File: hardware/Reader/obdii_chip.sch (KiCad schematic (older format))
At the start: 29 parts

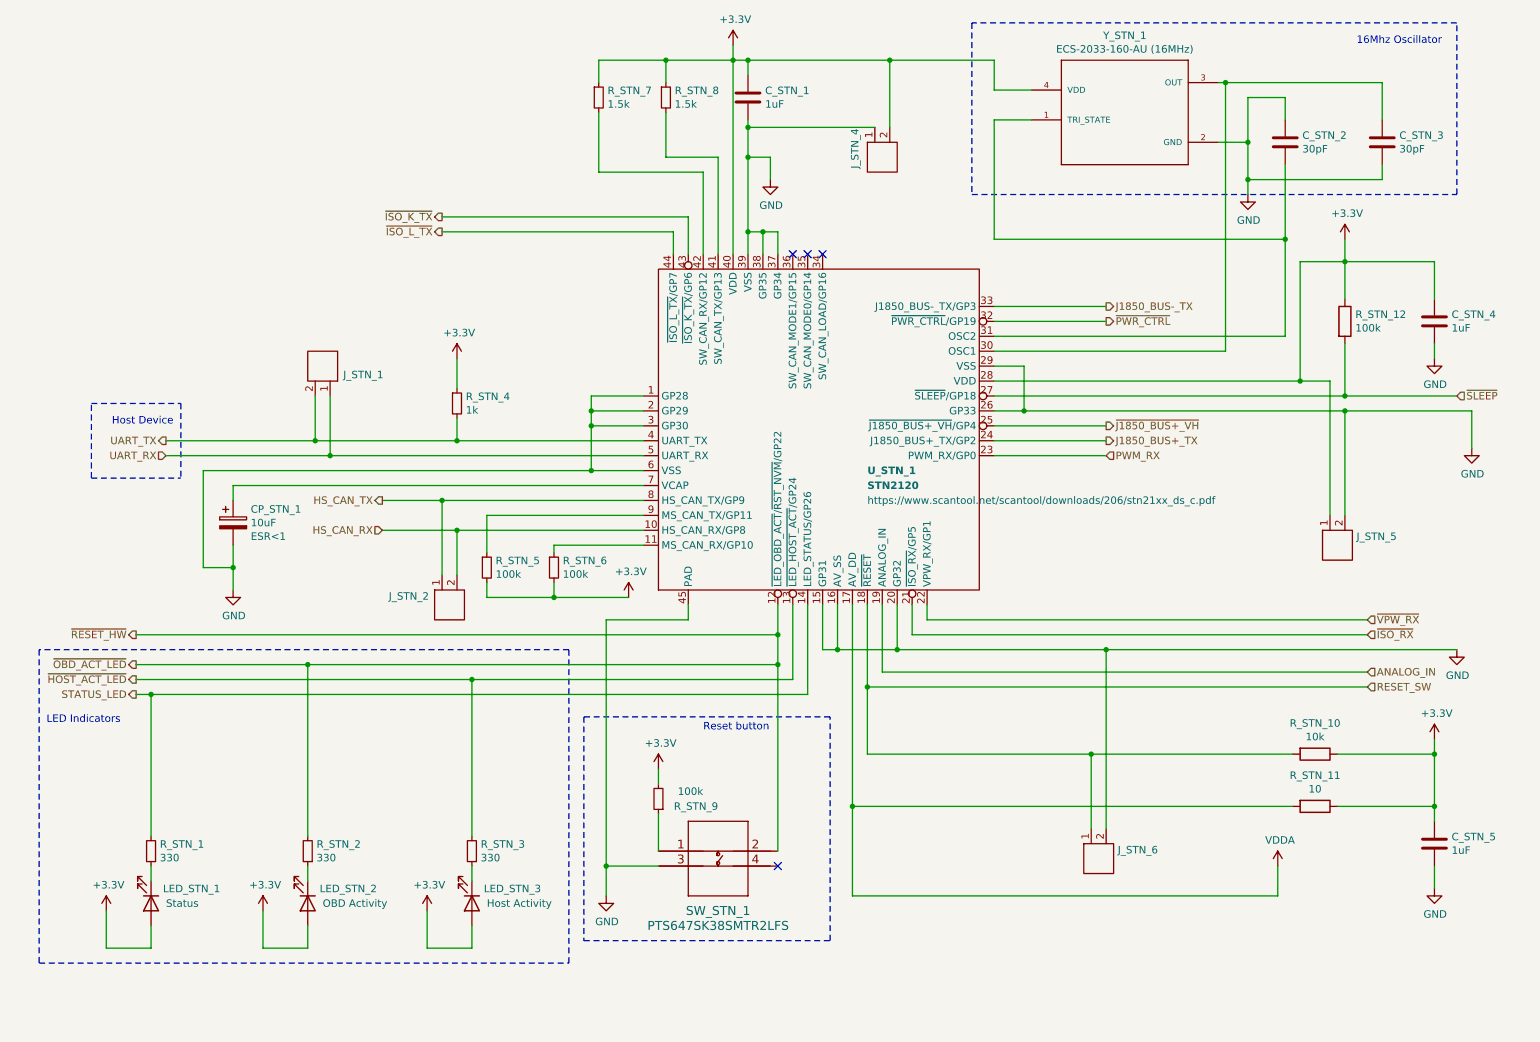
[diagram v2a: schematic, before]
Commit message: Updated schematic and gerber to v0.0.05. Added ESP32. Removed MS CAN and SW CAN Transceivers. Added silkscreen text to header pins. Improved readability
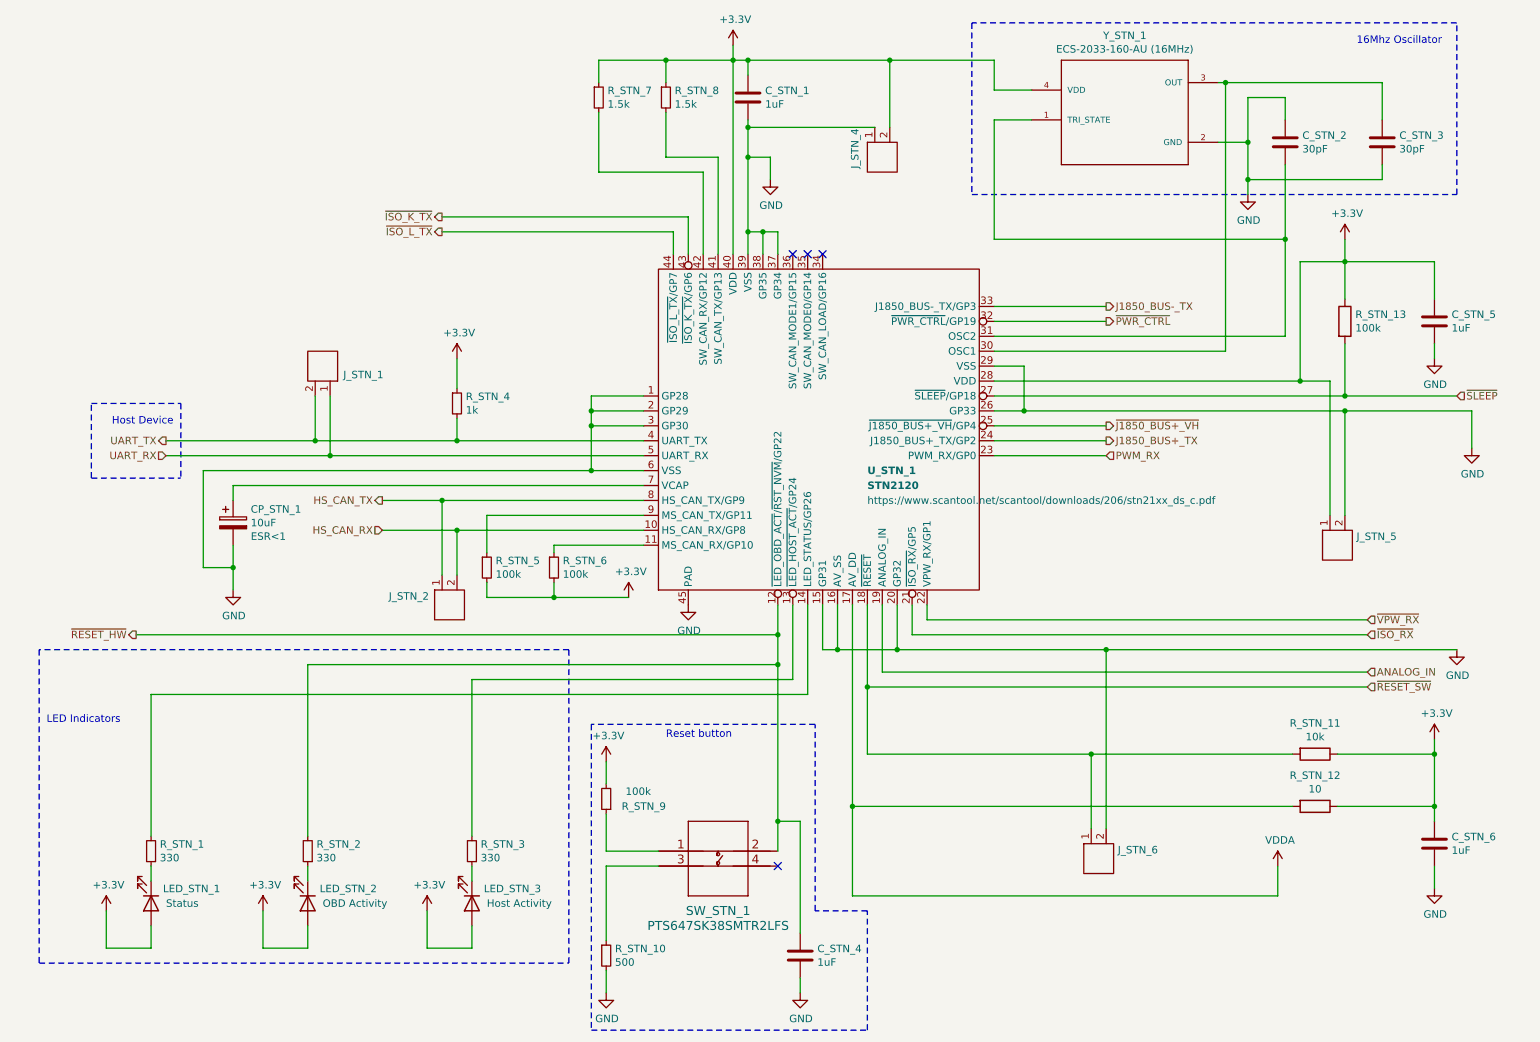
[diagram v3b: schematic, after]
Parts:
- added C_STN_4: 1uF, footprints:0603, symbol Device:C
- added R_STN_10: 500, footprints:RESC1508X55N, symbol Device:R_Small
- renumbered C_STN_4 to C_STN_5, C_STN_5 to C_STN_6, R_STN_10 to R_STN_11, R_STN_11 to R_STN_12, R_STN_12 to R_STN_13
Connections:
- net GND: now also C_STN_4.2, R_STN_10.2; no longer SW_STN_1.3
- net RESET_SW renamed ~RESET_SW~
- net STATUS_LED: no longer names the net of R_STN_1.2, U_STN_1.14 (LED_STATUS/GP26)
- net ~HOST_ACT_LED~: no longer names the net of R_STN_3.2, U_STN_1.13 (~LED_HOST_ACT~/GP24)
- net ~OBD_ACT_LED~ renamed ~RESET_HW~
- net ~RESET_HW~: now also C_STN_4.1
- new net: R_STN_10.1, SW_STN_1.3
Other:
- moved on the sheet: R_STN_9
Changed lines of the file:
@@
 Sheet 17 17
 Title "CANnect Reader | OBDII Chip (STN2110)"
-Date "2020-11-27"
+Date "2020-11-29"
 Rev "0.0.05"
 Comp "CANtech"
@@
 HS_CAN_RX
 $Comp
-L power:GND #PWR061
-U 1 1 5FC1071B
-P 4500 6550
-F 0 "#PWR061" H 4500 6300 50  0001 C CNN
-F 1 "GND" H 4505 6377 50  0000 C CNN
-F 2 "" H 4500 6550 50  0001 C CNN
-F 3 "" H 4500 6550 50  0001 C CNN
-	1    4500 6550
-	1    0    0    -1
-$EndComp
-$Comp
 L power:+3.3V #PWR064
 U 1 1 5FC11757
-P 4850 5700
-F 0 "#PWR064" H 4850 5550 50  0001 C CNN
-F 1 "+3.3V" H 4865 5873 50  0000 C CNN
-F 2 "" H 4850 5700 50  0001 C CNN
-F 3 "" H 4850 5700 50  0001 C CNN
-	1    4850 5700
+P 4500 5650
+F 0 "#PWR064" H 4500 5500 50  0001 C CNN
+F 1 "+3.3V" H 4515 5823 50  0000 C CNN
+F 2 "" H 4500 5650 50  0001 C CNN
+F 3 "" H 4500 5650 50  0001 C CNN
+	1    4500 5650
 	1    0    0    -1
 $EndComp
@@
 $EndComp
 Text HLabel 9600 5150 2    50   Input ~ 0
-RESET_SW
+~RESET_SW~
 Text HLabel 9600 5050 2    50   Input ~ 0
 ANALOG_IN
@@
 	5650 4800 5650 5000
 Connection ~ 5650 4800
-Text HLabel 1350 5200 0    50   Output ~ 0
-STATUS_LED
-Text HLabel 1350 5100 0    50   Output ~ 0
-~HOST_ACT_LED~
 Text HLabel 1350 4800 0    50   Output ~ 0
 ~RESET_HW~
-Text HLabel 1350 5000 0    50   Output ~ 0
-~OBD_ACT_LED~
 Wire Wire Line
 	1150 6900 1450 6900
 Wire Wire Line
 	1350 4800 5650 4800
-Wire Wire Line
-	1350 5100 3600 5100
-Wire Wire Line
-	1350 5200 1450 5200
 Wire Notes Line
 	700  4900 700  7000
@@
 Wire Wire Line
 	6150 5950 6150 6550
-Connection ~ 1450 5200
-Connection ~ 2500 5000
-Wire Wire Line
-	2500 5000 1350 5000
 Wire Wire Line
 	1450 5200 5850 5200
@@
 	4250 4900 700  4900
 Wire Wire Line
-	5050 4600 5050 4700
-Wire Wire Line
 	7100 2700 7850 2700
 Wire Wire Line
@@
 Wire Wire Line
 	3600 6150 3600 5100
-Connection ~ 3600 5100
 Wire Wire Line
 	3600 5100 5750 5100
@@
 L Device:R_Small R_STN_9
 U 1 1 5FC10F0A
-P 4850 5900
-F 0 "R_STN_9" H 4450 5950 50  0000 L CNN
-F 1 "100k" H 4550 5850 50  0000 L CNN
-F 2 "footprints:RESC1608X55N" H 4850 5900 50  0001 C CNN
-F 3 "https://www.yageo.com/upload/media/product/productsearch/datasheet/rchip/PYu-RT_1-to-0.01_RoHS_L_12.pdf" H 4850 5900 50  0001 C CNN
-F 4 "RT0603DRE07100KL" H 4850 5900 50  0001 C CNN "Part Name"
-F 5 "Yageo" H 4850 5900 50  0001 C CNN "Manufacturer"
-F 6 "DigiKey Canada" H 4850 5900 50  0001 C CNN "Vendor"
-F 7 "311-2395-1-ND" H 4850 5900 50  0001 C CNN "digikeypn"
-	1    4850 5900
+P 4500 5900
+F 0 "R_STN_9" H 4100 5950 50  0000 L CNN
+F 1 "100k" H 4200 5850 50  0000 L CNN
+F 2 "footprints:RESC1608X55N" H 4500 5900 50  0001 C CNN
+F 3 "https://www.yageo.com/upload/media/product/productsearch/datasheet/rchip/PYu-RT_1-to-0.01_RoHS_L_12.pdf" H 4500 5900 50  0001 C CNN
+F 4 "RT0603DRE07100KL" H 4500 5900 50  0001 C CNN "Part Name"
+F 5 "Yageo" H 4500 5900 50  0001 C CNN "Manufacturer"
+F 6 "DigiKey Canada" H 4500 5900 50  0001 C CNN "Vendor"
+F 7 "311-2395-1-ND" H 4500 5900 50  0001 C CNN "digikeypn"
+	1    4500 5900
 	-1   0    0    1
 $EndComp
@@
 $EndComp
 $Comp
-L Device:R R_STN_12
+L Device:R R_STN_13
 U 1 1 5FCC1888
 P 9450 2700
-F 0 "R_STN_12" H 9520 2746 50  0000 L CNN
+F 0 "R_STN_13" H 9520 2746 50  0000 L CNN
 F 1 "100k" H 9520 2655 50  0000 L CNN
 F 2 "footprints:RESC1608X55N" V 9380 2700 50  0001 C CNN
@@
 $EndComp
 $Comp
-L Device:C C_STN_4
+L Device:C C_STN_5
 U 1 1 5FCC9B8F
 P 10050 2700
-F 0 "C_STN_4" H 10165 2746 50  0000 L CNN
+F 0 "C_STN_5" H 10165 2746 50  0000 L CNN
 F 1 "1uF" H 10165 2655 50  0000 L CNN
 F 2 "footprints:0603" H 10088 2550 50  0001 C CNN
@@
 $EndComp
 $Comp
-L Device:C C_STN_5
+L Device:C C_STN_6
 U 1 1 5FC6BE46
 P 10050 6200
-F 0 "C_STN_5" H 10165 6246 50  0000 L CNN
+F 0 "C_STN_6" H 10165 6246 50  0000 L CNN
 F 1 "1uF" H 10165 6155 50  0000 L CNN
 F 2 "footprints:0603" H 10088 6050 50  0001 C CNN
@@
 $EndComp
 $Comp
-L Device:R R_STN_10
+L Device:R R_STN_11
 U 1 1 5FC6FB41
 P 9250 5600
-F 0 "R_STN_10" V 9043 5600 50  0000 C CNN
+F 0 "R_STN_11" V 9043 5600 50  0000 C CNN
 F 1 "10k" V 9134 5600 50  0000 C CNN
 F 2 "footprints:RESC1608X55N" V 9180 5600 50  0001 C CNN
@@
 $EndComp
 $Comp
-L Device:R R_STN_11
+L Device:R R_STN_12
 U 1 1 5FC6FCEB
 P 9250 5950
-F 0 "R_STN_11" V 9043 5950 50  0000 C CNN
+F 0 "R_STN_12" V 9043 5950 50  0000 C CNN
 F 1 "10" V 9134 5950 50  0000 C CNN
 F 2 "footprints:RESC1608X55N" V 9180 5950 50  0001 C CNN
@@
 Wire Wire Line
 	4150 4550 4650 4550
-Wire Notes Line
-	4350 5350 4350 6850
-Wire Notes Line
-	4350 6850 6000 6850
-Wire Notes Line
-	6000 6850 6000 5350
-Wire Notes Line
-	6000 5350 4350 5350
-Text Notes 5150 5450 0    50   ~ 0
+Text Notes 4900 5500 0    50   ~ 0
 Reset button
-Wire Wire Line
-	5050 4700 4500 4700
-Wire Wire Line
-	4500 4700 4500 6350
-Connection ~ 4500 6350
-Wire Wire Line
-	4500 6350 4500 6550
-Wire Wire Line
-	5650 5000 5650 6250
 $Comp
 L PTS647SK38SMTR2LFS:PTS647SK38SMTR2LFS SW_STN_1
@@
 Wire Wire Line
 	4500 6350 4850 6350
-Wire Wire Line
-	4850 5700 4850 5800
-Wire Wire Line
-	4850 6000 4850 6250
 NoConn ~ 5650 6350
+$Comp
+L Device:R_Small R_STN_10
+U 1 1 5FC65094
+P 4500 6950
+F 0 "R_STN_10" H 4559 6996 50  0000 L CNN
+F 1 "500" H 4559 6905 50  0000 L CNN
+F 2 "footprints:RESC1508X55N" H 4500 6950 50  0001 C CNN
+F 3 "https://www.vishay.com/docs/28916/mcxhp.pdf" H 4500 6950 50  0001 C CNN
+F 4 "Vishay" H 4500 6950 50  0001 C CNN "Manufacturer"
+F 5 "MCT0603PD4990DP500" H 4500 6950 50  0001 C CNN "Part Name"
+F 6 "DigiKey Canada" H 4500 6950 50  0001 C CNN "Vendor"
+F 7 "749-1523-1-ND" H 4500 6950 50  0001 C CNN "digikeypn"
+	1    4500 6950
+	1    0    0    -1
+$EndComp
+Wire Wire Line
+	4500 6350 4500 6850
+Wire Wire Line
+	4500 7050 4500 7200
+$Comp
+L power:GND #PWR061
+U 1 1 5FC1071B
+P 4500 7200
+F 0 "#PWR061" H 4500 6950 50  0001 C CNN
+F 1 "GND" H 4505 7027 50  0000 C CNN
+F 2 "" H 4500 7200 50  0001 C CNN
+F 3 "" H 4500 7200 50  0001 C CNN
+	1    4500 7200
+	1    0    0    -1
+$EndComp
+$Comp
+L power:GND #PWR0113
+U 1 1 5FC920A5
+P 5050 4600
+F 0 "#PWR0113" H 5050 4350 50  0001 C CNN
+F 1 "GND" H 5055 4427 50  0000 C CNN
+F 2 "" H 5050 4600 50  0001 C CNN
+F 3 "" H 5050 4600 50  0001 C CNN
+	1    5050 4600
+	1    0    0    -1
+$EndComp
+Wire Wire Line
+	4500 6000 4500 6250
+Wire Wire Line
+	4500 6250 4850 6250
+Wire Wire Line
+	4500 5650 4500 5800
+$Comp
+L Device:C C_STN_4
+U 1 1 5FCA7216
+P 5800 6950
+F 0 "C_STN_4" H 5915 6996 50  0000 L CNN
+F 1 "1uF" H 5915 6905 50  0000 L CNN
+F 2 "footprints:0603" H 5838 6800 50  0001 C CNN
+F 3 "https://content.kemet.com/datasheets/KEM_C1002_X7R_SMD.pdf" H 5800 6950 50  0001 C CNN
+F 4 "C0603C105K4RACTU" H 5800 6950 50  0001 C CNN "Part Name"
+F 5 "Kermet" H 5800 6950 50  0001 C CNN "Manufacturer"
+F 6 "DigiKey Canada" H 5800 6950 50  0001 C CNN "Vendor"
+F 7 "399-7847-1-ND" H 5800 6950 50  0001 C CNN "digikeypn"
+	1    5800 6950
+	1    0    0    -1
+$EndComp
+Wire Wire Line
+	5650 5000 5650 6050
+Wire Wire Line
+	5800 6800 5800 6050
+Wire Wire Line
+	5800 6050 5650 6050
+Connection ~ 5650 6050
+Wire Wire Line
+	5650 6050 5650 6250
+$Comp
+L power:GND #PWR0114
+U 1 1 5FCB987A
+P 5800 7200
+F 0 "#PWR0114" H 5800 6950 50  0001 C CNN
+F 1 "GND" H 5805 7027 50  0000 C CNN
+F 2 "" H 5800 7200 50  0001 C CNN
+F 3 "" H 5800 7200 50  0001 C CNN
+	1    5800 7200
+	1    0    0    -1
+$EndComp
+Wire Wire Line
+	5800 7200 5800 7100
+Wire Notes Line
+	4400 5400 4400 7450
+Wire Notes Line
+	4400 7450 6250 7450
+Wire Notes Line
+	6250 7450 6250 6650
+Wire Notes Line
+	6250 6650 5900 6650
+Wire Notes Line
+	5900 6650 5900 5400
+Wire Notes Line
+	5900 5400 4400 5400
 $EndSCHEMATC
